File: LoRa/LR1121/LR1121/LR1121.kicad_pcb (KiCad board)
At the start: 4 copper layers, 50 x 75 mm, 44 parts, among them J1 USB_B_Micro, J2 Con_GPS, SW1 NRST, SW2 BOOT0, U1 LBAA0XV2GT, U2 STM32L552CCUx, U3 MT29F4G01ABAFDWB-IT:F TR, U4 PCMF1USB3S, U5 MAX-M10S, U6 LTC4162IUFD-FFSM_PBF, Y1 32.768KHz, Y2 25MHz

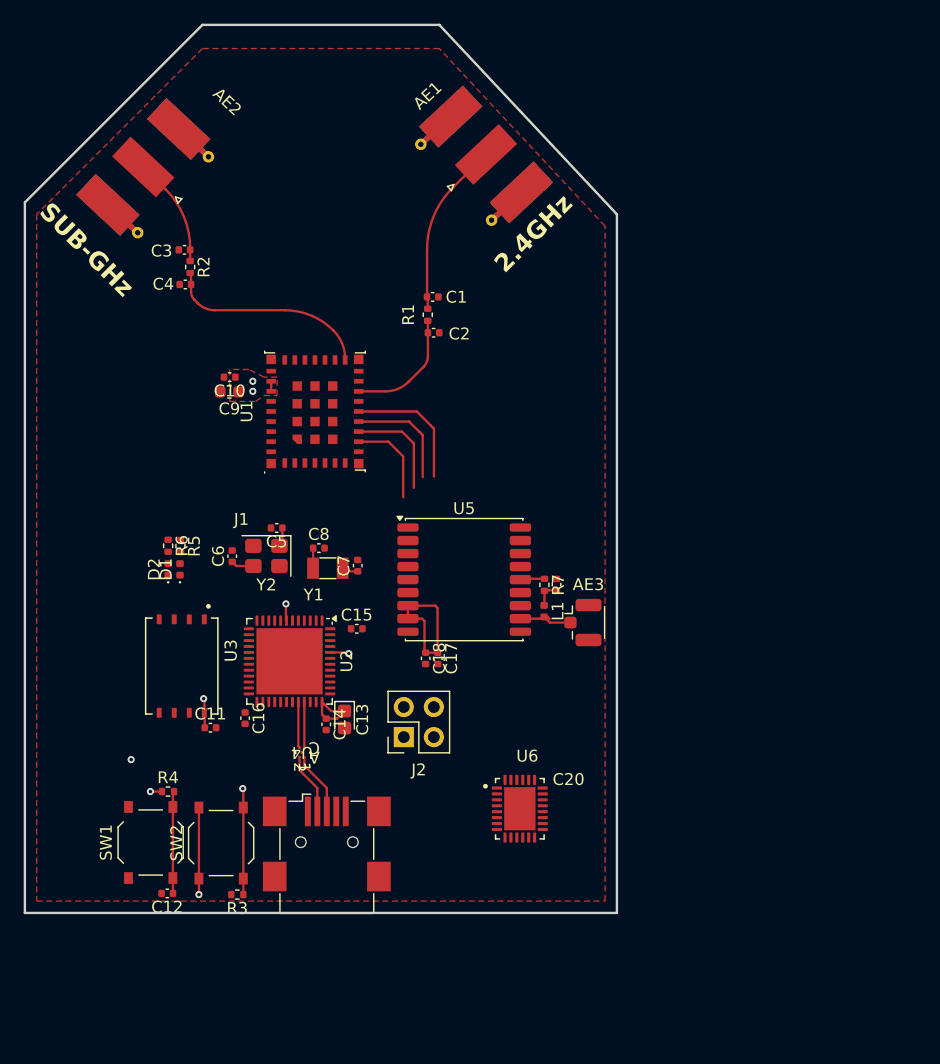
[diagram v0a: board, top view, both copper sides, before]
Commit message: [PCB] Inster power module in the PCB
It was improve the power module
.
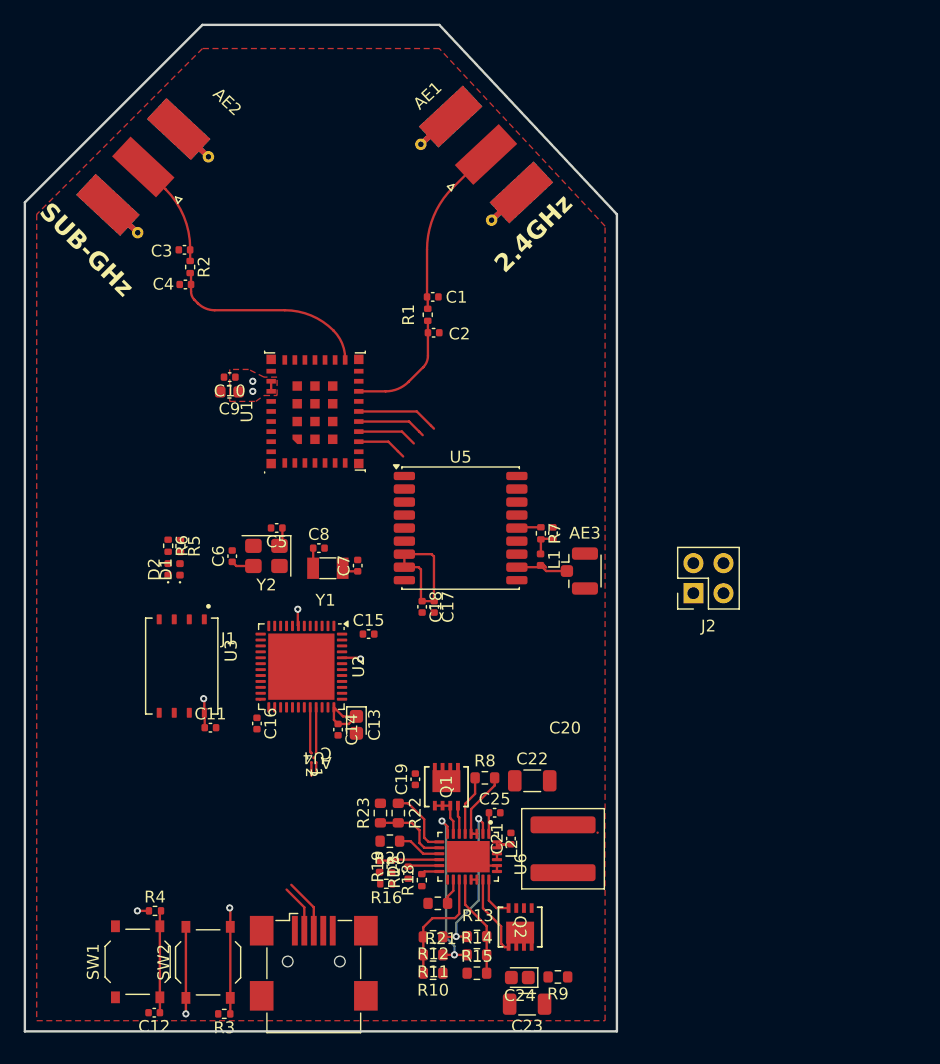
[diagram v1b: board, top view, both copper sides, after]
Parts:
- added C19: 100nF, Capacitor_SMD:C_0402_1005Metric, F.Cu at (133.0, 152.7)
- added C21: 100nF, Capacitor_SMD:C_0402_1005Metric, F.Cu at (141.1, 157.7)
- added C22: 10uF, Capacitor_SMD:C_1206_3216Metric, F.Cu at (142.8, 152.8)
- added C23: 10uF, Capacitor_SMD:C_1206_3216Metric, F.Cu at (142.4, 171.7)
- added C24: 150uF, Capacitor_Tantalum_SMD:CP_EIA-1608-10_AVX-L, F.Cu at (141.8, 169.5)
- added C25: 0.022uF, Capacitor_SMD:C_0402_1005Metric, F.Cu at (139.7, 155.5)
- added D3: RED, LED_SMD:LED_0402_1005Metric, F.Cu at (130.0, 160.1)
- added L2: 6.8uH, Inductor_SMD:L_Coilcraft_XAL6060-XXX, F.Cu at (145.4, 158.6)
- added Q1: FDMC8327L, _W_LoRa:WDFN8_511DR_OSI, F.Cu at (135.6, 153.3)
- added Q2: FDMC8327L, _W_LoRa:WDFN8_511DR_OSI, F.Cu at (141.8, 165.2)
- added R10: 0, Resistor_SMD:R_0603_1608Metric, F.Cu at (134.5, 169.1)
- added R11: 0, Resistor_SMD:R_0603_1608Metric, F.Cu at (134.5, 167.5)
- added R12: 0, Resistor_SMD:R_0603_1608Metric, F.Cu at (134.5, 166.0)
- added R13: 0, Resistor_SMD:R_0603_1608Metric, F.Cu at (138.2, 166.0)
- added R14: 0, Resistor_SMD:R_0603_1608Metric, F.Cu at (138.2, 167.5)
- added R15: 0, Resistor_SMD:R_0603_1608Metric, F.Cu at (138.2, 169.1)
- added R16: 2.2K, Resistor_SMD:R_0402_1005Metric, F.Cu at (130.5, 161.5)
- added R17: 4.7K, Resistor_SMD:R_0402_1005Metric, F.Cu at (132.4, 160.6)
- added R18: 4.7K, Resistor_SMD:R_0402_1005Metric, F.Cu at (133.5, 161.2)
- added R19: 100K, Resistor_SMD:R_0402_1005Metric, F.Cu at (131.0, 160.1)
- added R20: 63.4K, Resistor_SMD:R_0603_1608Metric, F.Cu at (130.8, 157.9)
- added R21: 10K, Resistor_SMD:R_0603_1608Metric, F.Cu at (134.9, 163.2)
- added R22: 10k, Resistor_SMD:R_0603_1608Metric, F.Cu at (131.5, 155.6)
- added R23: 10k, Resistor_SMD:R_0603_1608Metric, F.Cu at (130.0, 155.6)
- added R8: 0.01, Resistor_SMD:R_0603_1608Metric, F.Cu at (138.8, 152.6)
- added R9: 0.01, Resistor_SMD:R_0603_1608Metric, F.Cu at (145.0, 169.4)
- moved J2 27.3 mm to (156.5, 137.0)
- moved C12 10.1 mm to (110.9, 172.4)
- moved SW2 10.1 mm to (115.5, 168.2)
- moved R3 10.1 mm to (116.8, 172.5)
- moved J1 10.1 mm to (124.4, 168.1)
- moved R4 10.1 mm to (111.0, 163.8)
- moved SW1 10.1 mm to (109.5, 168.1)
- moved U6 5.95 mm to (137.4, 159.2), turned to -90 degrees
- moved C20 4.36 mm to (144.6, 131.9)
- moved AE3 4.36 mm to (146.8, 135.1)
- moved C17 4.36 mm to (134.6, 138.2)
- moved C18 4.36 mm to (133.6, 138.2)
- moved L1 4.36 mm to (143.6, 134.2)
- moved R7 4.36 mm to (143.6, 131.9)
- moved U5 4.36 mm to (136.8, 131.5)
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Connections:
- net Net-(U6-SW-Pad25) renamed /LoRa-system/SW
- U6 pad 1: unconnected-(U6-BOOST-Pad1) -> /LoRa-system/BOOST
- U6 pad 10: unconnected-(U6-NTC-Pad10) -> /LoRa-system/NTC
- U6 pad 11: unconnected-(U6-RT-Pad11) -> Net-(U6-RT)
- U6 pad 12: unconnected-(U6-~{SMBALERT}-Pad12) -> /LoRa-system/SMBALERT#
- U6 pad 13: unconnected-(U6-SCL-Pad13) -> /LoRa-system/I2C_SCL_MIC
- U6 pad 14: unconnected-(U6-SDA-Pad14) -> /LoRa-system/I2C_SDA_MIC
- U6 pad 15: unconnected-(U6-DVCC-Pad15) -> /LoRa-system/DVCC
- U6 pad 16: unconnected-(U6-SYNC-Pad16) -> /LoRa-system/SYNC
- U6 pad 17: unconnected-(U6-CELLS0-Pad17) -> /LoRa-system/CELLS0
- U6 pad 18: unconnected-(U6-CELLS1-Pad18) -> /LoRa-system/CELLS1
- U6 pad 19: unconnected-(U6-BATSENS+-Pad19) -> /LoRa-system/BATSENS+
- U6 pad 2: unconnected-(U6-INTVCC-Pad2) -> /LoRa-system/INTVCC
- U6 pad 20: unconnected-(U6-CSN-Pad20) -> /LoRa-system/BATSENS+
- U6 pad 21: unconnected-(U6-CSP-Pad21) -> /LoRa-system/CSP
- U6 pad 22: unconnected-(U6-BATFET-Pad22) -> /LoRa-system/BATFET
- U6 pad 23: Net-(U6-PGND-Pad23) -> GND
- U6 pad 24: Net-(U6-PGND-Pad23) -> GND
- U6 pad 27: Net-(U6-VOUT-Pad27) -> /LoRa-system/CLN
- U6 pad 28: Net-(U6-VOUT-Pad27) -> /LoRa-system/CLN
- U6 pad 29: unconnected-(U6-AGND-Pad29) -> GND
- U6 pad 3: unconnected-(U6-VOUTA-Pad3) -> /LoRa-system/CLN
- U6 pad 4: unconnected-(U6-CLN-Pad4) -> /LoRa-system/CLN
- U6 pad 5: unconnected-(U6-CLP-Pad5) -> /LoRa-system/CLP
- U6 pad 6: unconnected-(U6-INFET-Pad6) -> Net-(U6-INFET)
- U6 pad 7: unconnected-(U6-VIN-Pad7) -> /LoRa-system/VIN
- U6 pad 8: unconnected-(U6-VCC2P5-Pad8) -> /LoRa-system/VCC2P5
- U6 pad 9: unconnected-(U6-NTCBIAS-Pad9) -> /LoRa-system/NTCBIAS
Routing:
- net /LoRa-system/VCC2P5: track 0.00 -> 15.1 mm, vias 0 -> 2
- net /LoRa-system/INTVCC: track 0.00 -> 14.2 mm, vias 0 -> 2
- net /LoRa-system/CELLS0: track 0.00 -> 10.3 mm
- net /LoRa-system/CLN: track 0.00 -> 9.15 mm
- net /LoRa-system/CELLS1: track 0.00 -> 8.66 mm
- net /LoRa-system/CSP: track 0.00 -> 6.79 mm
- net /LoRa-system/NTC: track 0.00 -> 6.49 mm
- net /LoRa-system/NTCBIAS: track 0.00 -> 5.72 mm
- net /LoRa-system/SMBALERT#: track 0.00 -> 5.08 mm
- net /LoRa-system/CLP: track 0.00 -> 5.07 mm
- net /LoRa-system/LoRa_SCK: track 11.0 -> 6.95 mm
- net Net-(U6-RT): track 0.00 -> 3.79 mm
- net /LoRa-system/VIN: track 0.00 -> 3.78 mm
- net /LoRa-system/LoRa_MISO: track 8.81 -> 5.06 mm
- net /LoRa-system/BATFET: track 0.00 -> 3.70 mm
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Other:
- board size 50 x 75 mm -> 50 x 85 mm

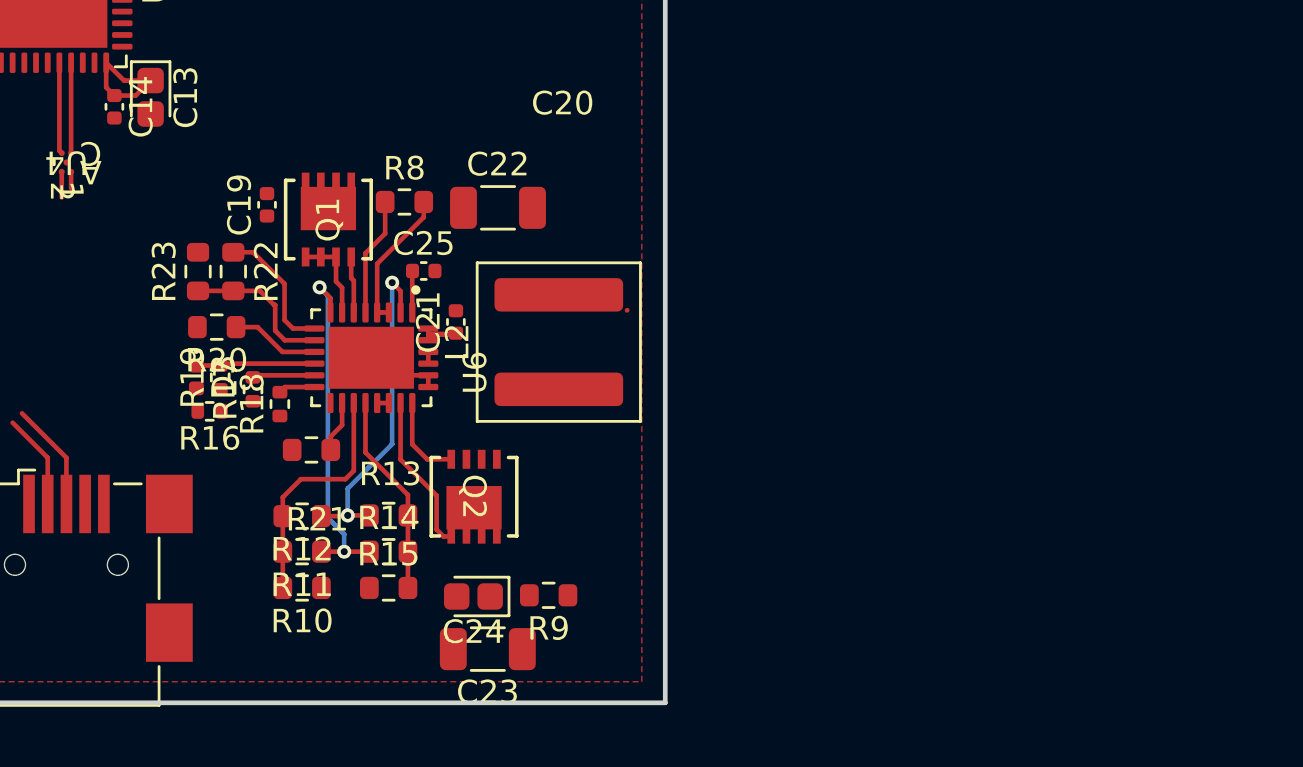
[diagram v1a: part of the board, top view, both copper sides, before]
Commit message: [PMIC] Changes PMIC chip to LTC4146 for BQ25619
The BQ25619 is now the PMIC because it had 3.5v-4.5v
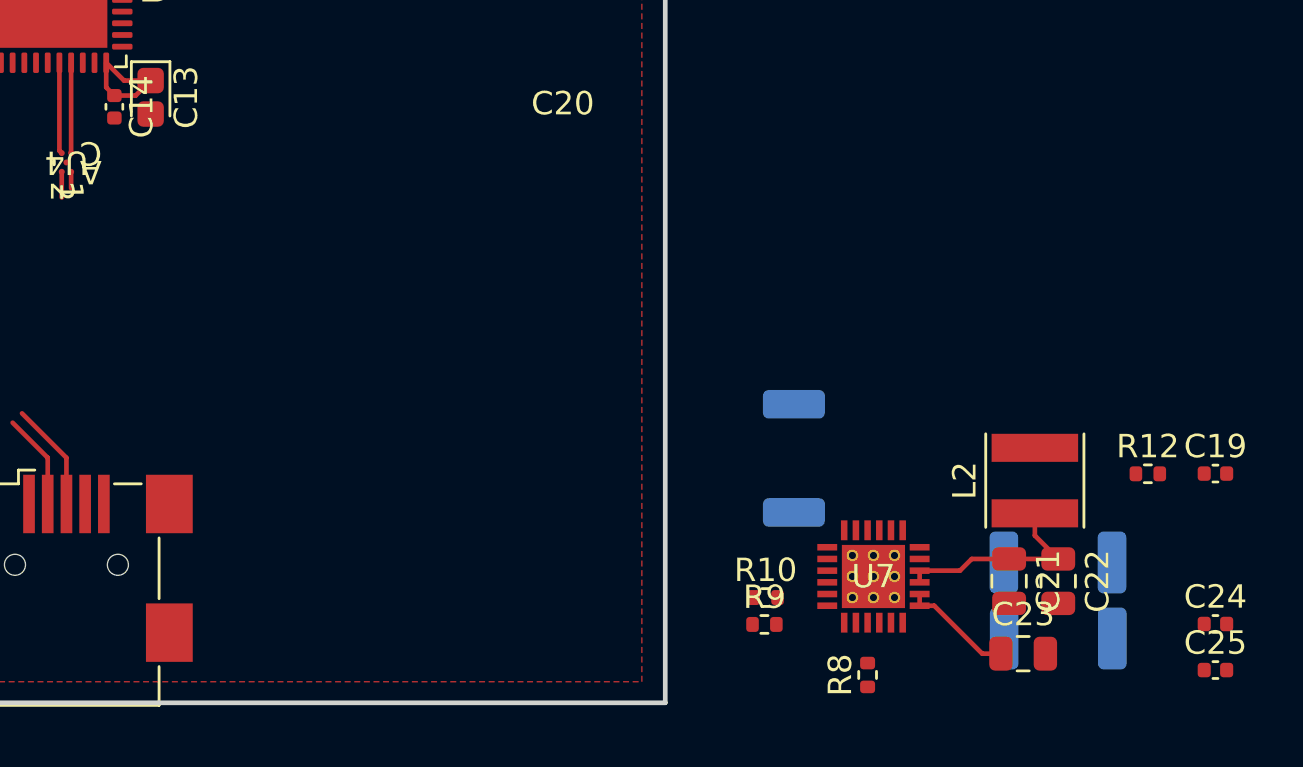
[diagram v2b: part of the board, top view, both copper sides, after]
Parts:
- removed D3: RED, LED_SMD:LED_0402_1005Metric
- removed Q1, Q2: FDMC8327L, _W_LoRa:WDFN8_511DR_OSI
- removed R15: 0, Resistor_SMD:R_0603_1608Metric
- removed R16: 2.2K, Resistor_SMD:R_0402_1005Metric
- removed R17, R18: 4.7K, Resistor_SMD:R_0402_1005Metric
- removed R19: 100K, Resistor_SMD:R_0402_1005Metric
- removed R20: 63.4K, Resistor_SMD:R_0603_1608Metric
- removed R21: 10K, Resistor_SMD:R_0603_1608Metric
- removed R22, R23: 10k, Resistor_SMD:R_0603_1608Metric
- removed U6: LTC4162IUFD-FFSM_PBF, _W_LoRa:QFN50P500X400X80-29N
- added U7: BQ25619ERTWR, _W_LoRa:BQ25619ERTWR, F.Cu at (158.9, 168.6)
- C19: value 100nF -> 1uF
- C21: value 100nF -> 10uF; footprint Capacitor_SMD:C_0402_1005Metric -> Capacitor_SMD:C_0805_2012Metric
- C22, C23: footprint Capacitor_SMD:C_1206_3216Metric -> Capacitor_SMD:C_0805_2012Metric
- C24: value 150uF -> 0.047uF; footprint Capacitor_Tantalum_SMD:CP_EIA-1608-10_AVX-L -> Capacitor_SMD:C_0402_1005Metric
- C25: value 0.022uF -> 0.1uF
- L2: value 6.8uH -> 2.2uH; footprint Inductor_SMD:L_Coilcraft_XAL6060-XXX -> Inductor_SMD:L_Taiyo-Yuden_MD-4040
- R10, R12: value 0 -> 10K; footprint Resistor_SMD:R_0603_1608Metric -> Resistor_SMD:R_0402_1005Metric
- R11, R13, R14: value 0 -> 0.01; footprint Resistor_SMD:R_0603_1608Metric -> Resistor_SMD:R_2010_5025Metric; moved to B.Cu
- R8, R9: value 0.01 -> 10K; footprint Resistor_SMD:R_0603_1608Metric -> Resistor_SMD:R_0402_1005Metric
- moved C19 42.1 mm to (173.5, 164.2), turned to 0 degrees
- moved C25 37.9 mm to (173.5, 172.6)
- moved R12 36.2 mm to (170.6, 164.2), turned to 0 degrees
- moved C24 31.7 mm to (173.5, 170.6), turned to 0 degrees
- moved R13 29.1 mm to (166.8, 171.2)
- moved C22 28.8 mm to (166.8, 168.8), turned to -90 degrees
- moved R14 28.6 mm to (166.8, 168.0)
- moved R8 28.3 mm to (158.7, 172.8), turned to 90 degrees
- moved C21 26.1 mm to (164.7, 168.8), turned to -90 degrees
- moved C23 22.9 mm to (165.3, 171.9), turned to 0 degrees
- moved R11 21.4 mm to (155.5, 163.6), turned to -90 degrees
- moved L2 21.2 mm to (165.8, 164.5)
- moved R10 19.8 mm to (154.3, 169.5), turned to 0 degrees
- moved R9 9.31 mm to (154.2, 170.7), turned to 0 degrees
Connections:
- C19 pad 1: /LoRa-system/VIN -> Net-(U7-VAC)
- C21 pad 1: /LoRa-system/CLN -> Net-(C21-Pad1)
- C22 pad 1: /LoRa-system/CLN -> Net-(C21-Pad1)
- C23 pad 1: /LoRa-system/BATSENS+ -> Net-(C23-Pad1)
- C24 pad 1: /LoRa-system/BATSENS+ -> Net-(C24-Pad1)
- C24 pad 2: GND -> Net-(U7-BTST)
- C25 pad 1: /LoRa-system/BOOST -> Net-(U7-BATSNS)
- C25 pad 2: /LoRa-system/SW -> GND
- J1 pad 1: unconnected-(J1-VBUS-Pad1) -> /LoRa-system/VIN
- L2 pad 1: /LoRa-system/CSP -> Net-(C21-Pad1)
- L2 pad 2: /LoRa-system/SW -> Net-(C24-Pad1)
- R10 pad 1: GND -> Net-(R10-Pad1)
- R10 pad 2: /LoRa-system/CELLS0 -> Net-(U7-SCL)
- R11 pad 1: /LoRa-system/VCC2P5 -> unconnected-(R11-Pad1)
- R11 pad 2: /LoRa-system/CELLS0 -> Net-(U7-VAC)
- R12 pad 1: /LoRa-system/INTVCC -> Net-(U7-VAC)
- R12 pad 2: /LoRa-system/CELLS0 -> GND
- R13 pad 1: /LoRa-system/INTVCC -> Net-(C23-Pad1)
- R13 pad 2: /LoRa-system/CELLS1 -> unconnected-(R13-Pad2)
- R14 pad 1: /LoRa-system/VCC2P5 -> Net-(C21-Pad1)
- R14 pad 2: /LoRa-system/CELLS1 -> unconnected-(R14-Pad2)
- R8 pad 1: /LoRa-system/CLP -> Net-(R10-Pad1)
- R8 pad 2: /LoRa-system/CLN -> Net-(U7-CE_N)
- R9 pad 1: /LoRa-system/CSP -> Net-(R10-Pad1)
- R9 pad 2: /LoRa-system/BATSENS+ -> Net-(U7-SDA)
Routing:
- net /LoRa-system/VCC2P5: track 15.1 -> 0.00 mm, vias 2 -> 0
- net /LoRa-system/INTVCC: track 14.2 -> 0.00 mm, vias 2 -> 0
- net /LoRa-system/CELLS0: track 10.3 -> 0.00 mm
- net /LoRa-system/CLN: track 9.15 -> 0.00 mm
- net Net-(C21-Pad1): track 0.00 -> 9.00 mm
- net /LoRa-system/CELLS1: track 8.66 -> 0.00 mm
- net /LoRa-system/CSP: track 6.79 -> 0.00 mm
- net /LoRa-system/NTC: track 6.49 -> 0.00 mm
- net /LoRa-system/NTCBIAS: track 5.72 -> 0.00 mm
- net /LoRa-system/SMBALERT#: track 5.08 -> 0.00 mm
- net /LoRa-system/CLP: track 5.07 -> 0.00 mm
- net Net-(C23-Pad1): track 0.00 -> 4.82 mm
- net Net-(U6-RT): track 3.79 -> 0.00 mm
- net /LoRa-system/VIN: track 3.78 -> 0.00 mm
- net /LoRa-system/BATFET: track 3.70 -> 0.00 mm
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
